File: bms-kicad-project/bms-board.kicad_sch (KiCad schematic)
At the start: 0 parts

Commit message: feat: schematic cleanup, continued layout
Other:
- sheet Battery Stack Monitor ports: added none; removed GNDCUR
- sheet External Connections and Sensing ports: added DAC_CLK, DAC_DAT, PIX_CLK, PIX_DAT; removed DACCLK, DACDAT, GNDCUR, PIXCLK, PIXDAT
- sheet Microcontroller ports: added DAC_CLK, DAC_DAT, PIX_CLK, PIX_DAT; removed DACCLK, DACDAT, PIXCLK, PIXDAT
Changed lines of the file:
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@@
-    (stroke (width 0) (type default))
-  )
-  (wire (pts (xy 224.79 85.09) (xy 292.1 85.09))
     (stroke (width 0) (type default))
   )
@@
       (effects (font (size 2.54 2.54)) (justify right))
     )
-    (pin "GNDCUR" output (at 224.79 85.09 0)
-      (effects (font (size 2.54 2.54)) (justify right))
-    )
     (pin "C2" input (at 181.61 143.51 180)
       (effects (font (size 2.54 2.54)) (justify left))
@@
       (effects (font (size 2.54 2.54)) (justify left))
     )
-    (pin "PIXDAT" bidirectional (at 359.41 144.78 0)
-      (effects (font (size 2.54 2.54)) (justify right))
-    )
-    (pin "PIXCLK" bidirectional (at 359.41 149.86 0)
+    (pin "PIX_DAT" bidirectional (at 359.41 144.78 0)
+      (effects (font (size 2.54 2.54)) (justify right))
+    )
+    (pin "PIX_CLK" bidirectional (at 359.41 149.86 0)
       (effects (font (size 2.54 2.54)) (justify right))
     )
@@
       (effects (font (size 2.54 2.54)) (justify right))
     )
-    (pin "DACCLK" bidirectional (at 359.41 137.16 0)
-      (effects (font (size 2.54 2.54)) (justify right))
-    )
-    (pin "DACDAT" bidirectional (at 359.41 133.35 0)
+    (pin "DAC_CLK" bidirectional (at 359.41 137.16 0)
+      (effects (font (size 2.54 2.54)) (justify right))
+    )
+    (pin "DAC_DAT" bidirectional (at 359.41 133.35 0)
       (effects (font (size 2.54 2.54)) (justify right))
     )
@@
       (effects (font (size 2.54 2.54)) (justify left top))
     )
-    (pin "PIXDAT" bidirectional (at 359.41 92.71 0)
-      (effects (font (size 2.54 2.54)) (justify right))
-    )
-    (pin "PIXCLK" bidirectional (at 359.41 87.63 0)
+    (pin "PIX_DAT" bidirectional (at 359.41 92.71 0)
+      (effects (font (size 2.54 2.54)) (justify right))
+    )
+    (pin "PIX_CLK" bidirectional (at 359.41 87.63 0)
       (effects (font (size 2.54 2.54)) (justify right))
     )
@@
       (effects (font (size 2.54 2.54)) (justify left))
     )
-    (pin "GNDCUR" input (at 292.1 85.09 180)
-      (effects (font (size 2.54 2.54)) (justify left))
-    )
     (pin "RGB_DIN" input (at 359.41 80.01 0)
       (effects (font (size 2.54 2.54)) (justify right))
     )
-    (pin "DACDAT" bidirectional (at 359.41 102.87 0)
-      (effects (font (size 2.54 2.54)) (justify right))
-    )
-    (pin "DACCLK" bidirectional (at 359.41 99.06 0)
-      (effects (font (size 2.54 2.54)) (justify right))
-    )
+    (pin "DAC_DAT" bidirectional (at 359.41 102.87 0)
+      (effects (font (size 2.54 2.54)) (justify right))
+    )
+    (pin "DAC_CLK" bidirectional (at 359.41 99.06 0)
+      (effects (font (size 2.54 2.54)) (justify right))
+    )

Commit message: feat: lotta layout
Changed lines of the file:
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@@
     (effects (font (size 2.54 2.54)) (justify left))
+  )
+  (text_box "TODO:\n- Link PGOOD between Microcontroller and 5V Regulator"
+    (at 374.65 237.49 0) (size 43.18 7.62)
+    (stroke (width 0) (type default))
+    (fill (type none))
+    (effects (font (size 1.27 1.27) (color 255 255 194 1)) (justify left top))
   )
   (text_box "5.25V\n10A"

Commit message: feat: big pre-design review schematic commit
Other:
- added sheet Power Tree (PowerTree.kicad_sch)
- sheet 5V Regulator ports: added PGOOD; removed none
- sheet External Connections and Sensing ports: added TEMP_BAL, TEMP_CORE; removed none
- sheet Microcontroller ports: added PGOOD, TEMP_BAL, TEMP_CORE; removed none

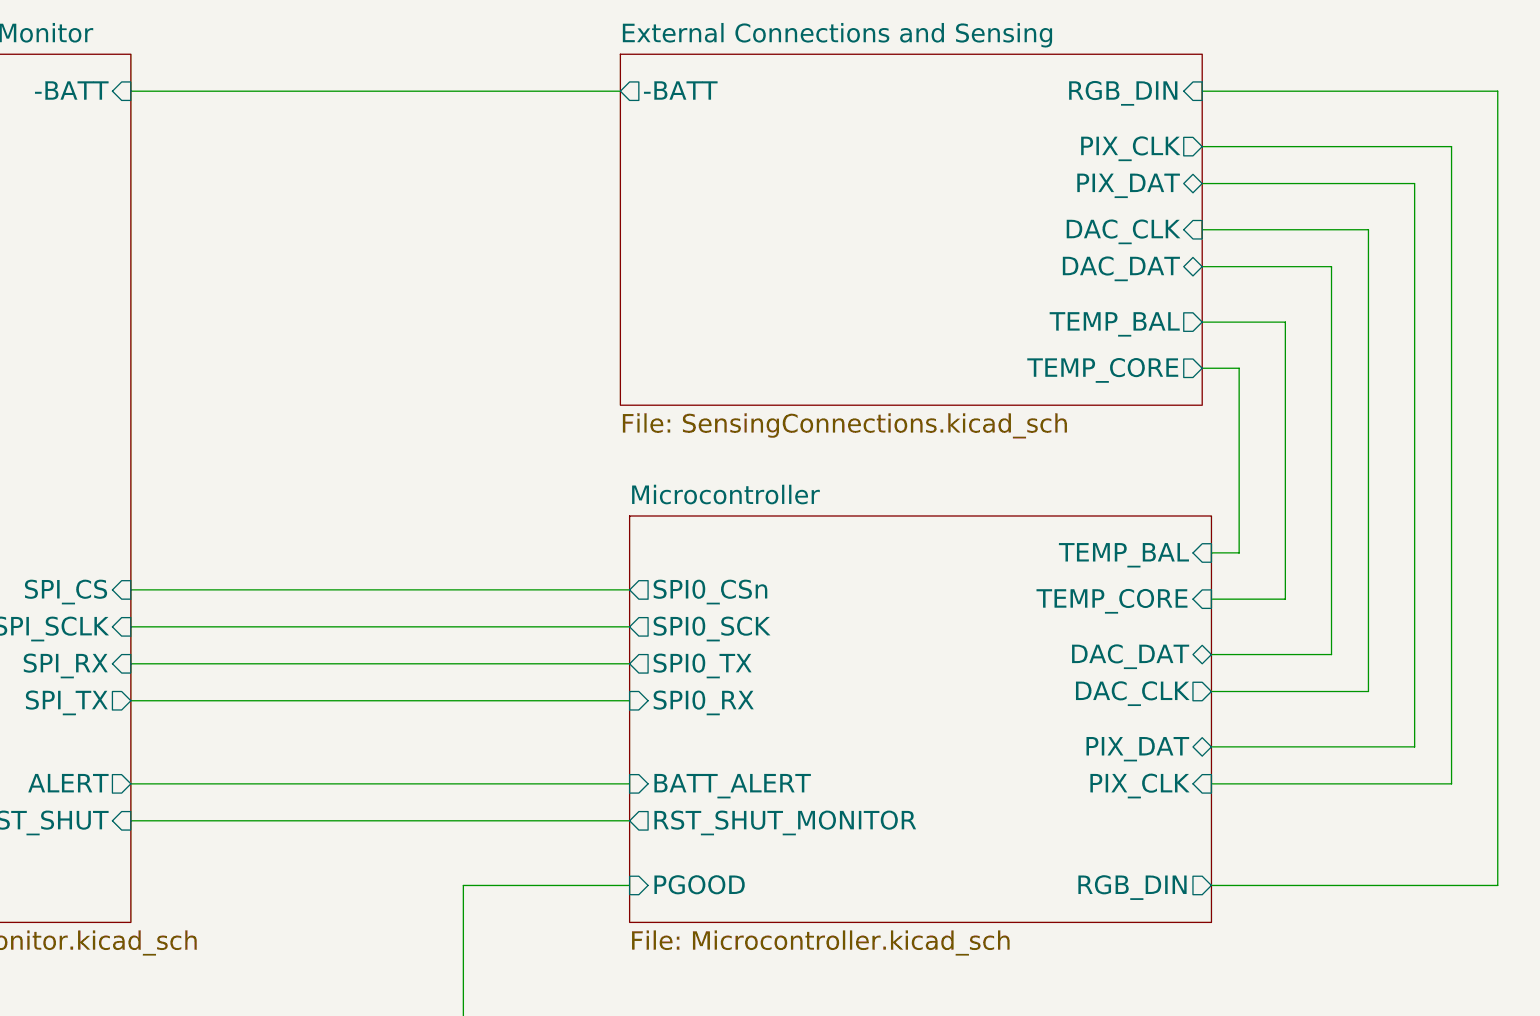
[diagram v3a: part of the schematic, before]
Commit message: feat: post-design review clarity
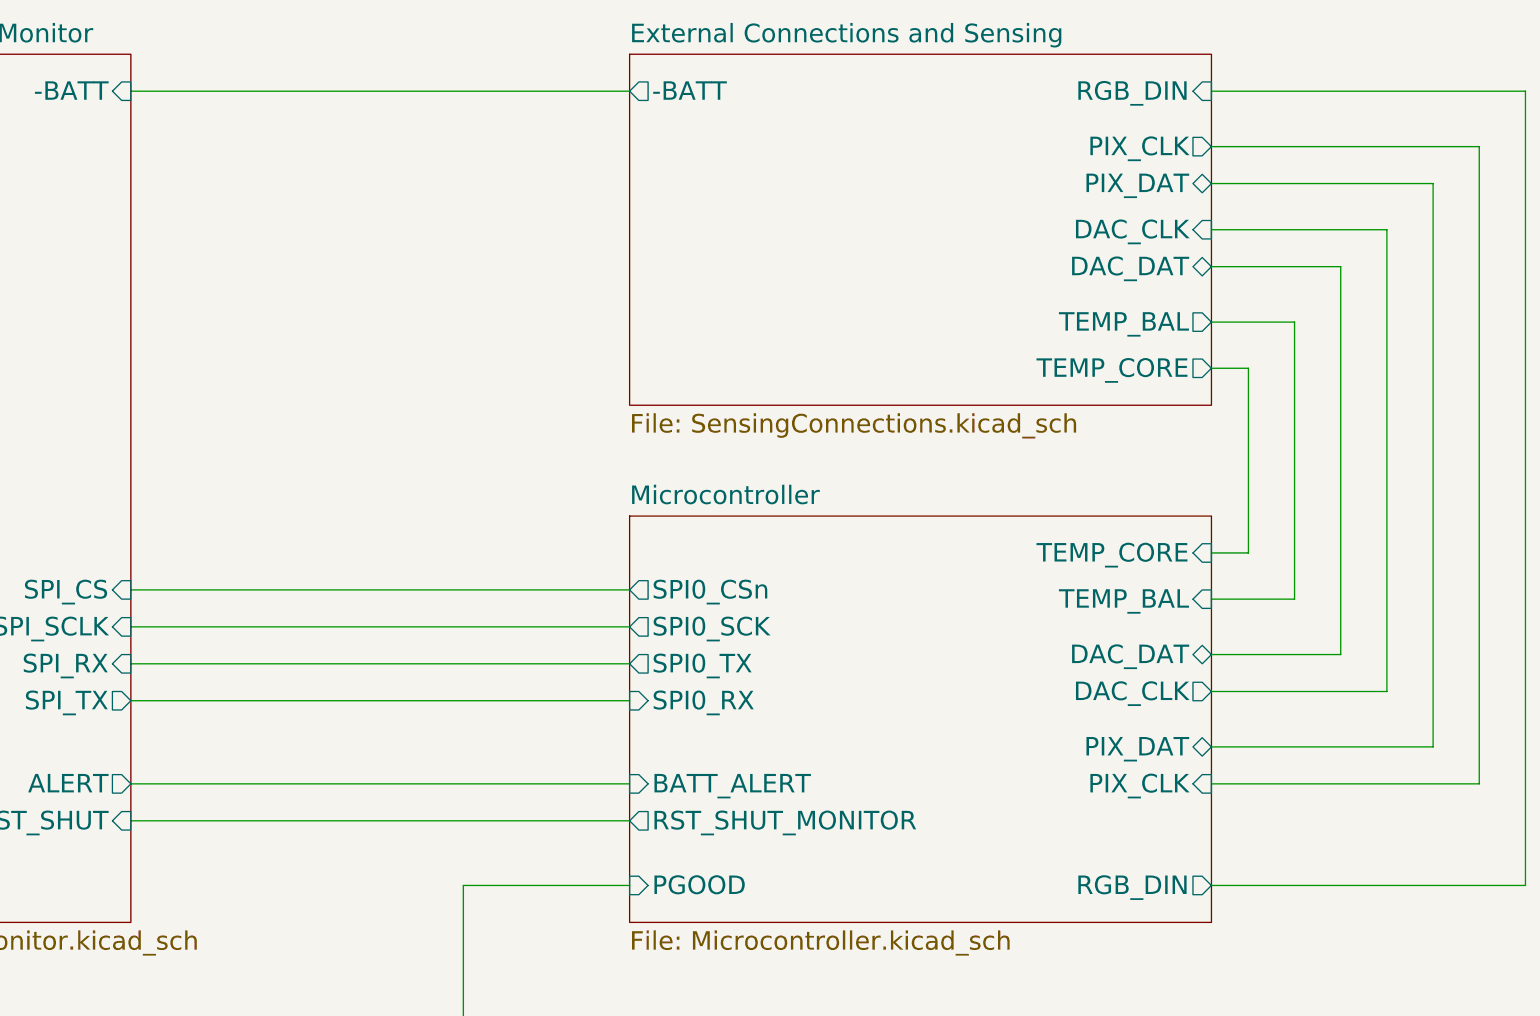
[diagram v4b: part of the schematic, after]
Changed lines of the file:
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@@
     (company "AeroNU - FixedWing")
   )
-  (wire (pts (xy 358.14 124.46) (xy 358.14 99.06))
+  (wire (pts (xy 359.41 124.46) (xy 359.41 99.06))
     (stroke (width 0) (type default))
   )
@@
     (stroke (width 0) (type default))
   )
-  (wire (pts (xy 353.06 60.96) (xy 393.7 60.96))
-    (stroke (width 0) (type default))
-  )
-  (wire (pts (xy 375.92 80.01) (xy 375.92 143.51))
-    (stroke (width 0) (type default))
-  )
-  (wire (pts (xy 358.14 99.06) (xy 353.06 99.06))
+  (wire (pts (xy 354.33 60.96) (xy 397.51 60.96))
+    (stroke (width 0) (type default))
+  )
+  (wire (pts (xy 378.46 80.01) (xy 378.46 143.51))
     (stroke (width 0) (type default))
   )
@@
     (stroke (width 0) (type default))
   )
-  (wire (pts (xy 354.33 156.21) (xy 387.35 156.21))
-    (stroke (width 0) (type default))
-  )
-  (wire (pts (xy 393.7 60.96) (xy 393.7 170.18))
-    (stroke (width 0) (type default))
-  )
-  (wire (pts (xy 393.7 170.18) (xy 354.33 170.18))
-    (stroke (width 0) (type default))
-  )
-  (wire (pts (xy 364.49 92.71) (xy 364.49 130.81))
-    (stroke (width 0) (type default))
-  )
-  (wire (pts (xy 387.35 68.58) (xy 387.35 156.21))
+  (wire (pts (xy 354.33 156.21) (xy 391.16 156.21))
+    (stroke (width 0) (type default))
+  )
+  (wire (pts (xy 397.51 60.96) (xy 397.51 170.18))
+    (stroke (width 0) (type default))
+  )
+  (wire (pts (xy 354.33 130.81) (xy 365.76 130.81))
+    (stroke (width 0) (type default))
+  )
+  (wire (pts (xy 397.51 170.18) (xy 354.33 170.18))
+    (stroke (width 0) (type default))
+  )
+  (wire (pts (xy 365.76 92.71) (xy 365.76 130.81))
+    (stroke (width 0) (type default))
+  )
+  (wire (pts (xy 391.16 68.58) (xy 391.16 156.21))
+    (stroke (width 0) (type default))
+  )
+  (wire (pts (xy 354.33 99.06) (xy 359.41 99.06))
     (stroke (width 0) (type default))
   )
@@
     (stroke (width 0) (type default))
   )
-  (wire (pts (xy 382.27 73.66) (xy 382.27 151.13))
+  (wire (pts (xy 384.81 73.66) (xy 384.81 151.13))
     (stroke (width 0) (type default))
   )
@@
     (stroke (width 0) (type default))
   )
-  (wire (pts (xy 370.84 138.43) (xy 354.33 138.43))
+  (wire (pts (xy 354.33 92.71) (xy 365.76 92.71))
+    (stroke (width 0) (type default))
+  )
+  (wire (pts (xy 372.11 138.43) (xy 354.33 138.43))
     (stroke (width 0) (type default))
   )
@@
     (stroke (width 0) (type default))
   )
-  (wire (pts (xy 353.06 80.01) (xy 375.92 80.01))
+  (wire (pts (xy 354.33 80.01) (xy 378.46 80.01))
     (stroke (width 0) (type default))
   )
@@
     (stroke (width 0) (type default))
   )
-  (wire (pts (xy 354.33 130.81) (xy 364.49 130.81))
-    (stroke (width 0) (type default))
-  )
   (wire (pts (xy 96.52 100.33) (xy 162.56 100.33))
     (stroke (width 0) (type default))
   )
-  (wire (pts (xy 205.74 60.96) (xy 273.05 60.96))
+  (wire (pts (xy 205.74 60.96) (xy 274.32 60.96))
     (stroke (width 0) (type default))
   )
@@
     (stroke (width 0) (type default))
   )
-  (wire (pts (xy 354.33 124.46) (xy 358.14 124.46))
-    (stroke (width 0) (type default))
-  )
-  (wire (pts (xy 354.33 151.13) (xy 382.27 151.13))
-    (stroke (width 0) (type default))
-  )
-  (wire (pts (xy 353.06 68.58) (xy 387.35 68.58))
-    (stroke (width 0) (type default))
-  )
-  (wire (pts (xy 353.06 92.71) (xy 364.49 92.71))
-    (stroke (width 0) (type default))
-  )
-  (wire (pts (xy 353.06 73.66) (xy 382.27 73.66))
+  (wire (pts (xy 354.33 151.13) (xy 384.81 151.13))
+    (stroke (width 0) (type default))
+  )
+  (wire (pts (xy 354.33 68.58) (xy 391.16 68.58))
+    (stroke (width 0) (type default))
+  )
+  (wire (pts (xy 354.33 124.46) (xy 359.41 124.46))
+    (stroke (width 0) (type default))
+  )
+  (wire (pts (xy 354.33 73.66) (xy 384.81 73.66))
     (stroke (width 0) (type default))
   )
@@
     (stroke (width 0) (type default))
   )
-  (wire (pts (xy 370.84 85.09) (xy 370.84 138.43))
+  (wire (pts (xy 372.11 85.09) (xy 372.11 138.43))
     (stroke (width 0) (type default))
   )
@@
     (stroke (width 0) (type default))
   )
-  (wire (pts (xy 353.06 85.09) (xy 370.84 85.09))
-    (stroke (width 0) (type default))
-  )
-  (wire (pts (xy 354.33 143.51) (xy 375.92 143.51))
+  (wire (pts (xy 354.33 85.09) (xy 372.11 85.09))
+    (stroke (width 0) (type default))
+  )
+  (wire (pts (xy 354.33 143.51) (xy 378.46 143.51))
     (stroke (width 0) (type default))
   )
@@
       (effects (font (size 2.54 2.54)) (justify right))
     )
-    (pin "TEMP_BAL" input (at 354.33 124.46 0)
+    (pin "TEMP_BAL" input (at 354.33 130.81 0)
       (effects (font (size 2.54 2.54)) (justify right))
     )
@@
       (effects (font (size 2.54 2.54)) (justify right))
     )
-    (pin "TEMP_CORE" input (at 354.33 130.81 0)
+    (pin "TEMP_CORE" input (at 354.33 124.46 0)
       (effects (font (size 2.54 2.54)) (justify right))
     )
@@
     )
   )
-  (sheet (at 273.05 55.88) (size 80.01 48.26) (fields_autoplaced)
-    (stroke (width 0.1524) (type solid))
-    (fill (color 0 0 0 0.0000))
-    (property "Sheetname" "External Connections and Sensing" (at 273.05 54.5334 0)
-      (effects (font (size 2.54 2.54)) (justify left bottom))
-    )
-    (property "Sheetfile" "SensingConnections.kicad_sch" (at 273.05 105.2326 0)
-      (effects (font (size 2.54 2.54)) (justify left top))
-    )
-    (pin "PIX_DAT" bidirectional (at 353.06 73.66 0)
-      (effects (font (size 2.54 2.54)) (justify right))
-    )
-    (pin "-BATT" output (at 273.05 60.96 180)
-      (effects (font (size 2.54 2.54)) (justify left))
-    )
-    (pin "RGB_DIN" input (at 353.06 60.96 0)
-      (effects (font (size 2.54 2.54)) (justify right))
-    )
-    (pin "DAC_DAT" bidirectional (at 353.06 85.09 0)
-      (effects (font (size 2.54 2.54)) (justify right))
-    )
-    (pin "DAC_CLK" input (at 353.06 80.01 0)
-      (effects (font (size 2.54 2.54)) (justify right))
-    )
-    (pin "PIX_CLK" output (at 353.06 68.58 0)
-      (effects (font (size 2.54 2.54)) (justify right))
-    )
-    (pin "TEMP_CORE" output (at 353.06 99.06 0)
-      (effects (font (size 2.54 2.54)) (justify right))
-    )
-    (pin "TEMP_BAL" output (at 353.06 92.71 0)
-      (effects (font (size 2.54 2.54)) (justify right))
-    )
+  (sheet (at 274.32 55.88) (size 80.01 48.26) (fields_autoplaced)
+    (stroke (width 0.1524) (type solid))
+    (fill (color 0 0 0 0.0000))
+    (property "Sheetname" "External Connections and Sensing" (at 274.32 54.5334 0)
+      (effects (font (size 2.54 2.54)) (justify left bottom))
+    )
+    (property "Sheetfile" "SensingConnections.kicad_sch" (at 274.32 105.2326 0)
+      (effects (font (size 2.54 2.54)) (justify left top))
+    )
+    (pin "PIX_DAT" bidirectional (at 354.33 73.66 0)
+      (effects (font (size 2.54 2.54)) (justify right))
+    )
+    (pin "-BATT" output (at 274.32 60.96 180)
+      (effects (font (size 2.54 2.54)) (justify left))
+    )
+    (pin "RGB_DIN" input (at 354.33 60.96 0)
+      (effects (font (size 2.54 2.54)) (justify right))
+    )
+    (pin "DAC_DAT" bidirectional (at 354.33 85.09 0)
+      (effects (font (size 2.54 2.54)) (justify right))
+    )
+    (pin "DAC_CLK" input (at 354.33 80.01 0)
+      (effects (font (size 2.54 2.54)) (justify right))
+    )
+    (pin "PIX_CLK" output (at 354.33 68.58 0)
+      (effects (font (size 2.54 2.54)) (justify right))
+    )
+    (pin "TEMP_CORE" output (at 354.33 99.06 0)
+      (effects (font (size 2.54 2.54)) (justify right))
+    )
+    (pin "TEMP_BAL" output (at 354.33 92.71 0)
+      (effects (font (size 2.54 2.54)) (justify right))
+    )

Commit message: feat: I am so tired. 4-layer layout almost done
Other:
- sheet External Connections and Sensing ports: added TEMP_ESC; removed TEMP_BAL
- sheet Microcontroller ports: added TEMP_ESC; removed TEMP_BAL
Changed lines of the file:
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@@
       (effects (font (size 2.54 2.54)) (justify right))
     )
-    (pin "TEMP_BAL" input (at 354.33 130.81 0)
+    (pin "TEMP_ESC" input (at 354.33 130.81 0)
       (effects (font (size 2.54 2.54)) (justify right))
     )
@@
       (effects (font (size 2.54 2.54)) (justify right))
     )
-    (pin "TEMP_BAL" output (at 354.33 92.71 0)
+    (pin "TEMP_ESC" output (at 354.33 92.71 0)
       (effects (font (size 2.54 2.54)) (justify right))
     )
